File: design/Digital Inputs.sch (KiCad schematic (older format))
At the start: 13 parts

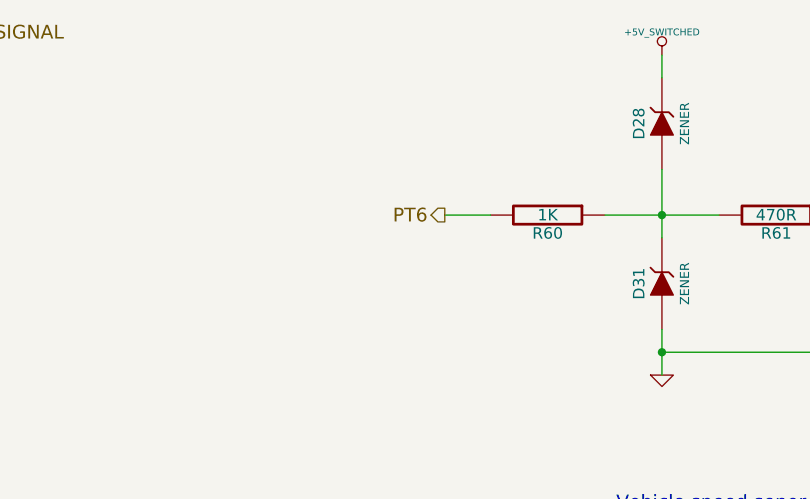
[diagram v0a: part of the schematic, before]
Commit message: revise schema according to Jaguar & Ravage project, eliminate as many errors as possible which were inherited from Puma board. Remove VSS interface, narrow band O2 interface, AC relay output, AC signal input. Make fuel injection configurable which can be batch fired or semi sequential fired
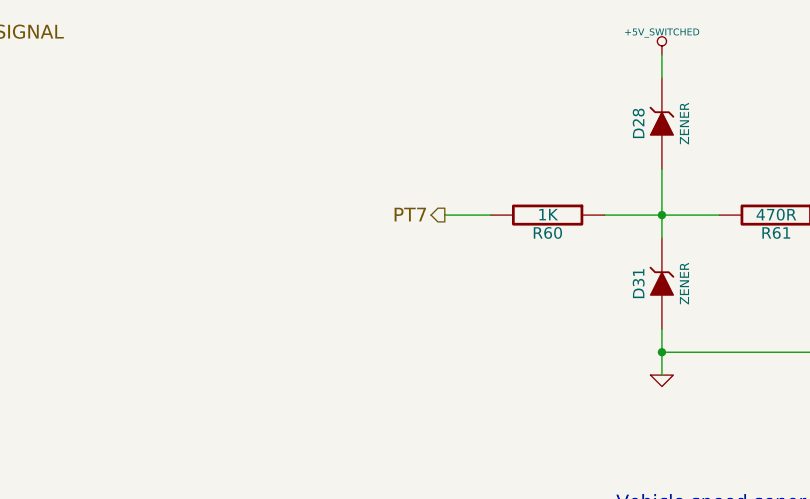
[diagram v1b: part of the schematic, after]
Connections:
- net PT6 renamed PT7
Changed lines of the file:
@@
-EESchema Schematic File Version 2  date 29/01/2012 19:39:37
+EESchema Schematic File Version 2  date 01/02/2012 17:26:48
 LIBS:power
 LIBS:device
@@
 EELAYER END
 $Descr A4 11700 8267
-Sheet 2 12
+Sheet 4 11
 Title "Digital Inputs"
-Date "24 jan 2012"
+Date "1 feb 2012"
 Rev "0.01"
 Comp "diyefi.org"
@@
 $EndComp
 Text HLabel 6350 3450 0    60   Output ~ 0
-PT6
+PT7
 $Comp
 L GND #PWR04
